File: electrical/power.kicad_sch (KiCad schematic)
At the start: 46 parts

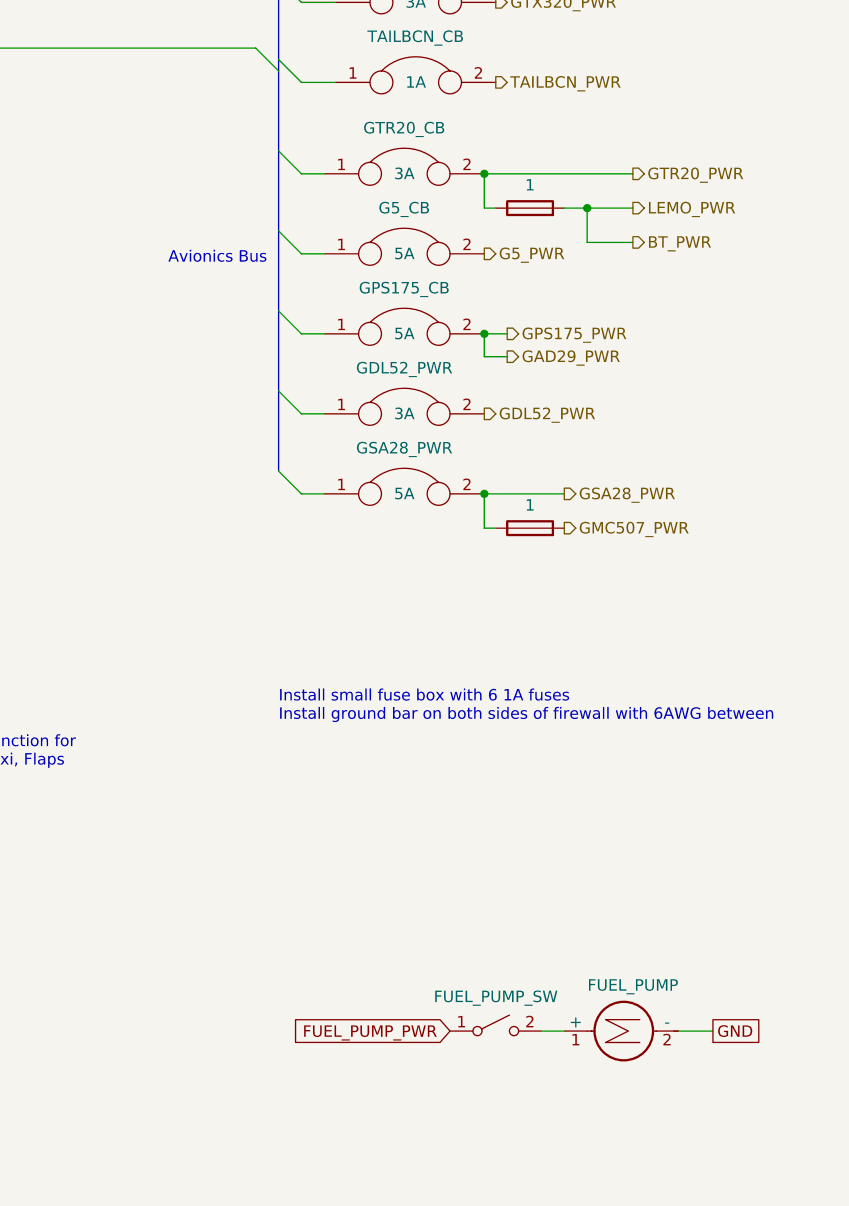
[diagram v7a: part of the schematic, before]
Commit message: Changed GTR CB to 7.5A. Added engine instrumentation. Added signal for fuel on.
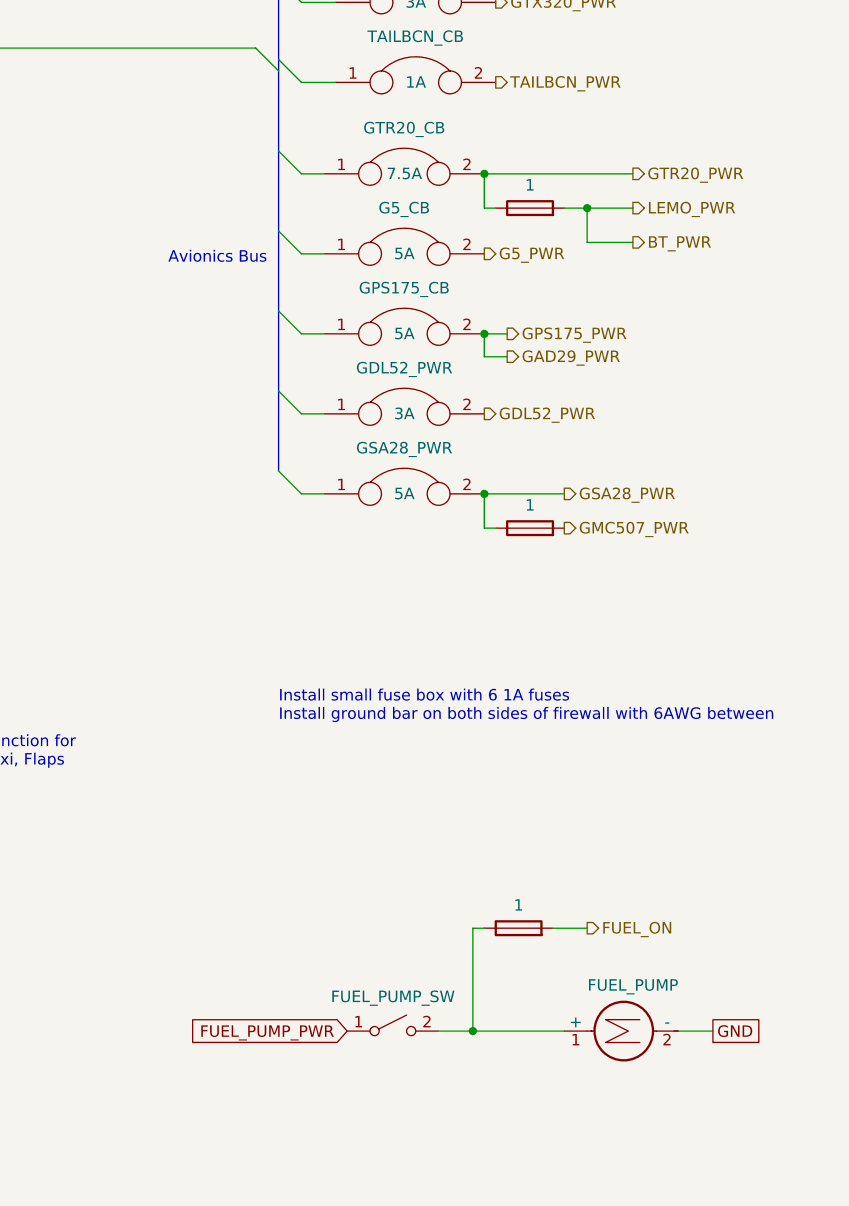
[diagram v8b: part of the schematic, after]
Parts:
- added FUEL_LT_FS: 1, symbol Device:Fuse
- GTR20_CB: value 3A -> 7.5A
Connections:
- net at FUEL_PUMP.1 (+), FUEL_PUMP_SW.2 (B): now also FUEL_LT_FS.1
- new net FUEL_ON: FUEL_LT_FS.2
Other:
- moved on the sheet: FUEL_PUMP_SW
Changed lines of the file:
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@@
   (title_block
     (title "Power Distribution")
-    (date "2024-02-15")
-    (rev "0.9.3")
+    (date "2024-05-02")
+    (rev "0.9.4")
     (company "N877RV")
   )
@@
   (junction (at 124.46 209.55) (diameter 0) (color 0 0 0 0)
   )
+  (junction (at 156.21 148.59) (diameter 0) (color 0 0 0 0)
+  )
   (bus_entry (at 48.26 242.57) (size 2.54 2.54)
     (stroke (width 0) (type default))
@@
     (stroke (width 0) (type default))
   )
-  (wire (pts (xy 163.83 148.59) (xy 166.37 148.59))
+  (wire (pts (xy 152.4 148.59) (xy 156.21 148.59))
     (stroke (width 0) (type default))
   )
@@
     (stroke (width 0) (type default))
   )
+  (wire (pts (xy 165.1 137.16) (xy 168.91 137.16))
+    (stroke (width 0) (type default))
+  )
   (wire (pts (xy 107.95 176.53) (xy 107.95 186.69))
     (stroke (width 0) (type default))
@@
     (stroke (width 0) (type default))
   )
+  (wire (pts (xy 156.21 148.59) (xy 166.37 148.59))
+    (stroke (width 0) (type default))
+  )
   (bus (pts (xy 57.15 30.48) (xy 57.15 36.83))
     (stroke (width 0) (type default))
@@
     (stroke (width 0) (type default))
   )
+  (wire (pts (xy 157.48 137.16) (xy 156.21 137.16))
+    (stroke (width 0) (type default))
+  )
+  (wire (pts (xy 179.07 148.59) (xy 182.88 148.59))
+    (stroke (width 0) (type default))
+  )
   (bus (pts (xy 57.15 95.25) (xy 57.15 104.14))
     (stroke (width 0) (type default))
@@
     (stroke (width 0) (type default))
   )
+  (wire (pts (xy 156.21 137.16) (xy 156.21 148.59))
+    (stroke (width 0) (type default))
+  )
   (wire (pts (xy 130.81 176.53) (xy 132.08 176.53))
     (stroke (width 0) (type default))
@@
   )
   (wire (pts (xy 36.83 78.74) (xy 38.1 78.74))
-    (stroke (width 0) (type default))
-  )
-  (wire (pts (xy 179.07 148.59) (xy 182.88 148.59))
     (stroke (width 0) (type default))
   )
@@
     )
   )
-  (global_label "FUEL_PUMP_PWR" (shape input) (at 153.67 148.59 180) (fields_autoplaced)
+  (global_label "FUEL_PUMP_PWR" (shape input) (at 142.24 148.59 180) (fields_autoplaced)
     (effects (font (size 1.27 1.27)) (justify right))
-    (property "Intersheetrefs" "${INTERSHEET_REFS}" (at 134.8401 148.59 0)
+    (property "Intersheetrefs" "${INTERSHEET_REFS}" (at 123.4101 148.59 0)
       (effects (font (size 1.27 1.27)) (justify right) hide)
     )
@@
   )
   (hierarchical_label "GDL52_PWR" (shape output) (at 157.48 80.01 0) (fields_autoplaced)
+    (effects (font (size 1.27 1.27)) (justify left))
+  )
+  (hierarchical_label "FUEL_ON" (shape output) (at 168.91 137.16 0) (fields_autoplaced)
     (effects (font (size 1.27 1.27)) (justify left))
   )
@@
     )
   )
+  (symbol (lib_id "Device:Fuse") (at 161.29 137.16 90) (unit 1)
+    (in_bom yes) (on_board yes) (dnp no)
+    (property "Reference" "FUEL_LT_FS" (at 161.29 133.35 90)
+      (effects (font (size 1.27 1.27)) hide)
+    )
+    (property "Value" "1" (at 161.29 134.62 90)
+      (effects (font (size 1.27 1.27)))
+    )
+    (property "Footprint" "" (at 161.29 138.938 90)
+      (effects (font (size 1.27 1.27)) hide)
+    )
+    (property "Datasheet" "~" (at 161.29 137.16 0)
+      (effects (font (size 1.27 1.27)) hide)
+    )
+    (pin "1")
+    (pin "2")
+    (instances
+      (project "electrical"
+        (path "/e8ec215a-dbe2-4eba-a577-e50a0a128049/2852c073-fbc9-4469-a6bf-ba3e911c7f5a"
+          (reference "FUEL_LT_FS") (unit 1)
+        )
+      )
+    )
+  )
   (symbol (lib_id "flyerx:Circuit_Breaker") (at 71.12 165.1 0) (unit 1)
     (in_bom yes) (on_board yes) (dnp no)
@@
     )
   )
-  (symbol (lib_id "Switch:SW_SPST") (at 158.75 148.59 0) (unit 1)
-    (in_bom yes) (on_board yes) (dnp no)
-    (property "Reference" "FUEL_PUMP_SW" (at 158.75 144.78 0)
-      (effects (font (size 1.27 1.27)))
-    )
-    (property "Value" "~" (at 158.75 144.78 0)
-      (effects (font (size 1.27 1.27)))
-    )
-    (property "Footprint" "" (at 158.75 148.59 0)
-      (effects (font (size 1.27 1.27)) hide)
-    )
-    (property "Datasheet" "~" (at 158.75 148.59 0)
+  (symbol (lib_id "Switch:SW_SPST") (at 147.32 148.59 0) (unit 1)
+    (in_bom yes) (on_board yes) (dnp no)
+    (property "Reference" "FUEL_PUMP_SW" (at 147.32 144.78 0)
+      (effects (font (size 1.27 1.27)))
+    )
+    (property "Value" "~" (at 147.32 144.78 0)
+      (effects (font (size 1.27 1.27)))
+    )
+    (property "Footprint" "" (at 147.32 148.59 0)
+      (effects (font (size 1.27 1.27)) hide)
+    )
+    (property "Datasheet" "~" (at 147.32 148.59 0)
       (effects (font (size 1.27 1.27)) hide)
     )
@@
       (effects (font (size 1.27 1.27)))
     )
-    (property "Value" "3A" (at 148.59 53.34 0)
-      (effects (font (size 1.27 1.27)))
-    )
+    (property "Value" "7.5A" (at 148.59 53.34 0)
+      (effects (font (size 1.27 1.27)))
+    )
